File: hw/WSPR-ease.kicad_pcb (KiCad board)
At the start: 4 copper layers, 99 x 64 mm, 140 parts, among them J101 pwr+data, J102 SMA, J103 SMA, K201 G6K-2, K202 G6K-2, K203 G6K-2, Q101 MMBF170, Q201 MMBF170, Q202 MMBF170, Q203 MMBF170, Q401 MMBF170, Q402 MMBF170, Q403 MMBF170, Q404 MMBF170, Q405 MMBF170, Q406 MMBF170, Q501 MMBF170, Q502 MMBF170, Q503 MMBF170, Q504 MMBF170, Q505 MMBF170, Q506 MMBF170, T301 BN-43-202_DualPri_CTSec, U101 SRV05-4, U102 ESP32-S3-WROOM-1-N8R8, U103 LMR51430YDDCR, U104 GNSS module, U105 TPS74612PQWDRBRQ1, U106 TPS22918DBVR, U301 ICE40UP5K-SG48ITR, U401 UCC27524DGN, U501 UCC27524DGN, Y301 40MHz

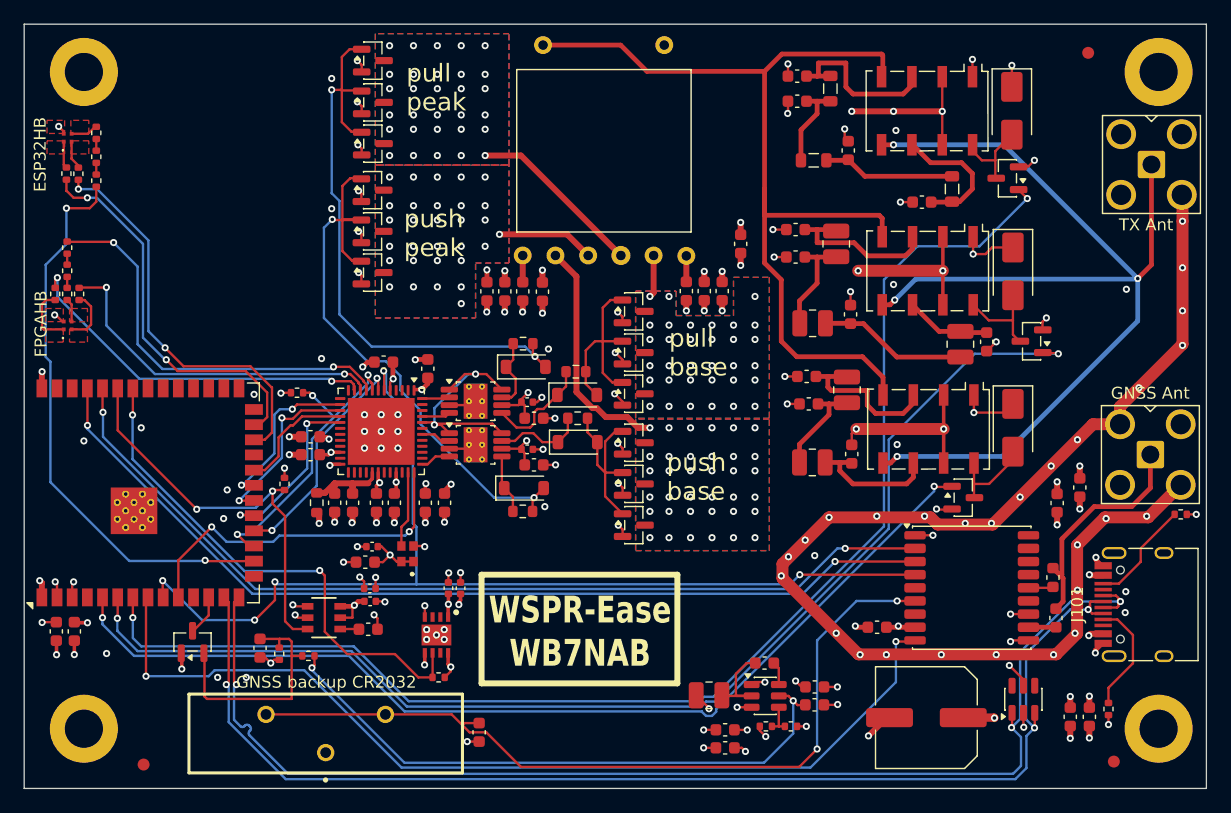
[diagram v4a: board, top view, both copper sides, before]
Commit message: Add symbols for new components, switch to SI5351 in place of FPGA. Simplify!
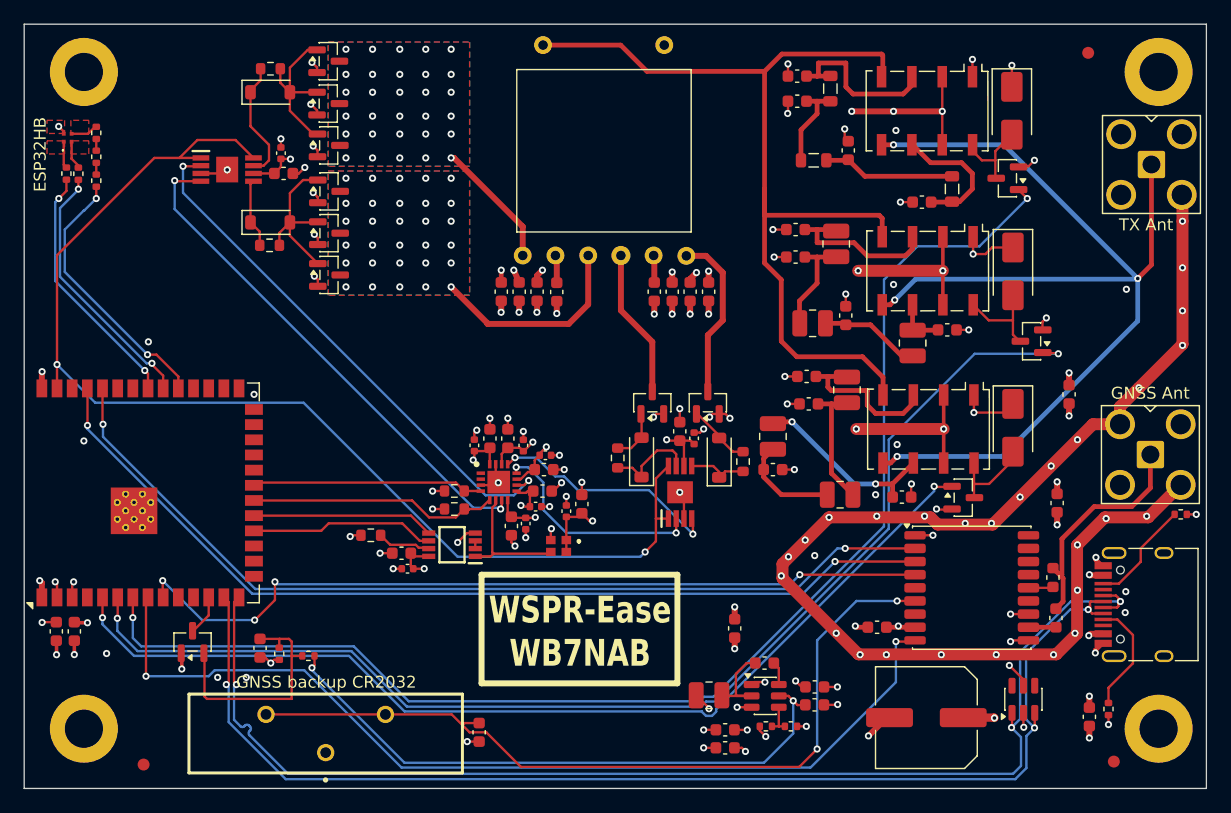
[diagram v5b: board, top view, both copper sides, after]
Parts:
- removed C115, C116, C401, C501: 1uF, Capacitor_SMD:C_0402_1005Metric
- removed C117: 1nF NP0 100V, Capacitor_SMD:C_0603_1608Metric
- removed the C206 at (118.8, 93.7)
- removed the C313 at (78.5, 116.7)
- removed the C314 at (86.1, 116.6)
- removed the C317 at (79.1, 109.5)
- removed the C318 at (84.8, 109.5)
- removed C402, C502: 100nF X7R 50V, Capacitor_SMD:C_0603_1608Metric
- removed D401, D402, D501, D502: 1N4148W, Diode_SMD:D_SOD-123
- removed the L205 at (128.0, 96.2)
- removed Q401, Q402, Q403, Q404, Q405, Q406, Q501, Q502, Q503, Q504, Q505, Q506: MMBF170, Package_TO_SOT_SMD:SOT-23
- removed the R110 at (84.3, 124.1)
- removed R113: 10k, Resistor_SMD:R_0402_1005Metric
- removed R401, R402, R501, R502: 10, Resistor_SMD:R_0603_1608Metric
- removed U105: TPS74612PQWDRBRQ1, Library:SON65P300X300X100-9N-D
- removed U106: TPS22918DBVR, Library:DBV6_TEX
- removed U401, U501: UCC27524DGN, Package_SO:Texas_DGN0008G_VSSOP-8-1EP_3x3mm_P0.65mm_EP2x2.94mm_Mask1.846x2.15mm_ThermalVias
- added C204: 910pF NP0 100V, Capacitor_SMD:C_0603_1608Metric, F.Cu at (123.1, 109.0)
- added C208: 330pF NP0 50V, Capacitor_SMD:C_0603_1608Metric, F.Cu at (126.9, 95.0)
- added C304: 1uF, Capacitor_SMD:C_0402_1005Metric, F.Cu at (81.7, 115.0)
- added C305: 100nF X7R 50V, Capacitor_SMD:C_0603_1608Metric, F.Cu at (81.2, 113.7)
- added C306: 1uF, Capacitor_SMD:C_0402_1005Metric, F.Cu at (71.1, 80.2)
- added C307: 100nF X7R 50V, Capacitor_SMD:C_0603_1608Metric, F.Cu at (71.3, 81.9)
- added C325: 100nF X7R 50V, Capacitor_SMD:C_0603_1608Metric, F.Cu at (90.1, 104.1)
- added C326: 1uF, Capacitor_SMD:C_0402_1005Metric, F.Cu at (91.4, 104.7)
- added C327: 100nF X7R 50V, Capacitor_SMD:C_0603_1608Metric, F.Cu at (93.1, 106.7)
- added C328: 1uF, Capacitor_SMD:C_0402_1005Metric, F.Cu at (93.2, 105.5)
- added D302: 1N4148W, Diode_SMD:D_SOD-123, F.Cu at (70.2, 75.1)
- added D303: 1N4148W, Diode_SMD:D_SOD-123, F.Cu at (107.8, 105.7)
- added D304: 1N4148W, Diode_SMD:D_SOD-123, F.Cu at (101.3, 105.7)
- added L203: 2.7uH, Inductor_SMD:L_1008_2520Metric, F.Cu at (112.3, 103.9)
- added L206: 1uH, Inductor_SMD:L_1008_2520Metric, F.Cu at (124.0, 96.1)
- added Q301: MMBF170, Package_TO_SOT_SMD:SOT-23, F.Cu at (75.1, 83.4)
- added Q302: MMBF170, Package_TO_SOT_SMD:SOT-23, F.Cu at (75.1, 86.9)
- added Q303: MMBF170, Package_TO_SOT_SMD:SOT-23, F.Cu at (75.1, 90.4)
- added Q304: MMBF170, Package_TO_SOT_SMD:SOT-23, F.Cu at (75.1, 72.5)
- added Q305: MMBF170, Package_TO_SOT_SMD:SOT-23, F.Cu at (75.1, 76.0)
- added Q306: MMBF170, Package_TO_SOT_SMD:SOT-23, F.Cu at (75.1, 79.5)
- added Q307: MMBF170, Package_TO_SOT_SMD:SOT-23, F.Cu at (106.8, 101.1)
- added Q308: MMBF170, Package_TO_SOT_SMD:SOT-23, F.Cu at (102.2, 101.1)
- added U302: UCC27525DGN, Library:SOP65P490X110-9N, F.Cu at (66.6, 81.6)
- added U303: UCC27525DGN, Library:SOP65P490X110-9N, F.Cu at (104.5, 108.6)
- added Y302: Si5351C-B-GM, Library:QFN50P300X300X90-17N-D, F.Cu at (89.3, 107.8)
- C201: value 470pF NP0 100V -> 910pF NP0 100V
- C202: value 1nF NP0 100V -> 1.6nF NP0 100V
- C203: value 470pF NP0 100V -> 1.6nF NP0 100V
- C205: renamed from C204; value 150pF NP0 100V -> 330pF NP0 50V
- C206: renamed from C205; value 330pF NP0 100V -> 560pF NP0 50V
- C207: value 150pF NP0 100V -> 560pF NP0 50V
- C315, C320: value 100nF X7R 50V -> 1uF; footprint Capacitor_SMD:C_0603_1608Metric -> Capacitor_SMD:C_0402_1005Metric
- C322, C324: value 10uF X5R 25V -> 1uF; footprint Capacitor_SMD:C_0603_1608Metric -> Capacitor_SMD:C_0402_1005Metric
- C323: value 10uF X5R 25V -> 100nF X7R 50V
- D301: value LED_BGRA -> 1N4148W; footprint Library:UHD111AFKAC3K23E1L3VG5ZB3Z3 -> Diode_SMD:D_SOD-123
- L201, L202: value 1.2uH -> 2.7uH
- L204: renamed from L203; value 560nH -> 1uH
- L205: renamed from L204; value 680nH -> 1.2uH
- R301, R303: value 100 -> 10; footprint Resistor_SMD:R_0402_1005Metric -> Resistor_SMD:R_0603_1608Metric
- R302: value 100 -> 10k; footprint Resistor_SMD:R_0402_1005Metric -> Resistor_SMD:R_0603_1608Metric
- R304, R305: value 100 -> 47; footprint Resistor_SMD:R_0402_1005Metric -> Resistor_SMD:R_0603_1608Metric
- R306: value 10k -> 5.1k; footprint Resistor_SMD:R_0402_1005Metric -> Resistor_SMD:R_0603_1608Metric
- R307: value 10 -> 5.1k
- U301: value ICE40UP5K-SG48ITR -> SN74LVC1G74DCTR; footprint Package_DFN_QFN:QFN-48-1EP_7x7mm_P0.5mm_EP5.6x5.6mm -> Library:SOP65P400X130-8N
- moved R304 57.3 mm to (109.8, 106.0), turned to 90 degrees
- moved R305 49.1 mm to (99.3, 105.7), turned to 90 degrees
- moved R302 33.7 mm to (78.6, 112.2), turned to 180 degrees
- moved C317 29.1 mm to (109.1, 120.0), turned to -90 degrees
- moved C315 26.8 mm to (105.7, 104.1), turned to -90 degrees
- moved R303 25.4 mm to (70.2, 73.1), turned to 0 degrees
- moved C316 21.7 mm to (104.5, 103.5)
- moved C324 19.7 mm to (92.4, 109.8)
- moved D301 19.0 mm to (70.2, 86.0), turned to 0 degrees
- moved C312 18.8 mm to (96.3, 109.6), turned to 90 degrees
- moved C321 17.9 mm to (90.4, 111.4), turned to -90 degrees
- moved R301 17.0 mm to (70.2, 87.9), turned to 0 degrees
- moved C311 16.5 mm to (95.0, 110.2), turned to 90 degrees
- moved R306 16.4 mm to (85.6, 110.0)
- moved C322 14.6 mm to (91.6, 111.2), turned to -90 degrees
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- renumbered C208 to C209, C209 to C210, C210 to C211, C211 to C212, C302 to C301, C303 to C302, C304 to C303, C310 to C308, C311 to C309, C312 to C310, C308 to C311, C309 to C312, C305 to C313, C301 to C314, C307 to C317, C306 to C318, L206 to L207, L207 to L208, L208 to L209, R111 to R110, R112 to R111
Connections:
- C311 pad 1: +VFPGAIO -> +3.3V
- C312 pad 1: +VFPGAIO -> +3.3V
- C315 pad 2: +VFPGACORE -> VBUS
- C316 pad 2: +VFPGAIO -> VBUS
- C319 pad 1: GND -> +3.3V
- C319 pad 2: Net-(U301D-VCCPLL) -> GND
- C320 pad 1: GND -> +3.3V
- C320 pad 2: +VFPGAIO -> GND
- C321 pad 1: GND -> +3.3V
- C321 pad 2: +VFPGAIO -> GND
- C322 pad 1: GND -> +3.3V
- C322 pad 2: Net-(U301D-VCCPLL) -> GND
- C323 pad 1: GND -> +3.3V
- C323 pad 2: +VFPGAIO -> GND
- C324 pad 1: GND -> +3.3V
- C324 pad 2: +VFPGAIO -> GND
- D301 pad 1: /Transmitter/blu -> Net-(D301-K)
- D301 pad 2: /Transmitter/grn -> Net-(D301-A)
- K201 pad 6: Net-(C203-Pad1) -> Net-(C204-Pad1)
- K202 pad 6: Net-(C207-Pad1) -> Net-(C208-Pad1)
- L205 pad 2: Net-(C206-Pad1) (its old number) -> Net-(C207-Pad1)
- R105 pad 1: Net-(U102-IO46) -> /hbRed
- R108 pad 1: Net-(U102-IO47) -> /hbGrn
- R109 pad 1: Net-(U102-IO48) -> /hbBlu
- R301 pad 1: /Transmitter/hbR -> Net-(D301-K)
- R301 pad 2: Net-(R301-Pad2) -> Net-(D301-A)
- R302 pad 1: Net-(R301-Pad2) -> Net-(U301-~{PRE})
- R302 pad 2: Net-(R302-Pad2) -> +3.3V
- R303 pad 1: Net-(R302-Pad2) -> Net-(D302-K)
- R303 pad 2: /Transmitter/red -> Net-(D302-A)
- R304 pad 1: /Transmitter/hbG -> Net-(D303-K)
- R304 pad 2: /Transmitter/grn -> Net-(D303-A)
- R305 pad 1: /Transmitter/hbB -> Net-(D304-K)
- R305 pad 2: /Transmitter/blu -> Net-(D304-A)
- R306 pad 1: /fpgaCRESET -> /txSDA
- R306 pad 2: GND -> +3.3V
- R307 pad 1: Net-(U301D-VCCPLL) -> /txSCL
- R307 pad 2: +VFPGACORE -> +3.3V
- T301 pad 1: VBUS -> /Transmitter/ahcPushT
- T301 pad 2: /Transmitter/pullBaseT -> VBUS
- T301 pad 3: /Transmitter/pullPeakT -> /Transmitter/ahcPullT
- T301 pad 4: /Transmitter/pushPeakT -> /Transmitter/txPullT
- T301 pad 5: /Transmitter/pushBaseT -> VBUS
- T301 pad 6: VBUS -> /Transmitter/txPushT
- U102 pad 10: /fpgaNRESET -> unconnected-(U102-IO17-Pad10)
- U102 pad 16: Net-(U102-IO46) -> unconnected-(U102-IO46-Pad16)
- U102 pad 17: /fpgaCRESET -> unconnected-(U102-IO9-Pad17)
- U102 pad 18: /fpgaDONE -> /txCLKen
- U102 pad 19: /fpgaMOSI -> /tcxoDiv2
- U102 pad 20: /fpgaSCLK -> /txSDA
- U102 pad 21: /fpgaMISO -> /txSCL
- U102 pad 22: /fpgaNCS -> unconnected-(U102-IO14-Pad22)
- U102 pad 24: Net-(U102-IO47) -> unconnected-(U102-IO47-Pad24)
- U102 pad 25: Net-(U102-IO48) -> unconnected-(U102-IO48-Pad25)
- U102 pad 31: unconnected-(U102-IO38-Pad31) -> /hbRed
- U102 pad 32: unconnected-(U102-IO39-Pad32) -> /hbGrn
- U102 pad 33: unconnected-(U102-IO40-Pad33) -> /hbBlu
- U102 pad 34: /pgFPGACORE -> unconnected-(U102-IO41-Pad34)
- U102 pad 35: /enFPGAIO -> unconnected-(U102-IO42-Pad35)
- U102 pad 39: unconnected-(U102-IO1-Pad39) -> /txPAen
- U301 pad 1: +VFPGAIO -> /Transmitter/tcxo
- U301 pad 2: unconnected-(U301C-IOB_6a-Pad2) -> Net-(U301-D)
- U301 pad 3: unconnected-(U301C-IOB_9b-Pad3) -> Net-(U301-D)
- U301 pad 4: unconnected-(U301C-IOB_8a-Pad4) -> GND
- U301 pad 5: +VFPGACORE -> /tcxoDiv2
- U301 pad 6: /gnssPPS -> /txCLKen
- U301 pad 7: /fpgaDONE -> Net-(U301-~{PRE})
- U301 pad 8: /fpgaCRESET -> +3.3V
- Y301 pad 1: +VFPGAIO -> +3.3V
- Y301 pad 3: /Transmitter/FPGACLK -> /Transmitter/tcxo
- Y301 pad 4: +VFPGAIO -> +3.3V
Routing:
- net /txPAen: track 0.00 -> 99.2 mm, vias 0 -> 2
- net Net-(D501-A): track 51.2 -> 0.00 mm, vias 2 -> 0
- net Net-(D402-A): track 49.5 -> 0.00 mm, vias 2 -> 0
- net Net-(U102-IO46): track 47.6 -> 0.00 mm, vias 2 -> 0
- net /Transmitter/txCLK1: track 0.00 -> 44.9 mm, vias 0 -> 2
- net /pgFPGACORE: track 43.5 -> 0.00 mm, vias 2 -> 0
- net /Transmitter/txCLK2: track 0.00 -> 43.1 mm, vias 0 -> 2
- net /Transmitter/hbR: track 34.5 -> 0.00 mm, vias 2 -> 0
- net /enFPGAIO: track 34.4 -> 0.00 mm, vias 2 -> 0
- net Net-(U102-IO47): track 33.9 -> 0.00 mm, vias 2 -> 0
- net Net-(U102-IO48): track 32.3 -> 0.00 mm, vias 2 -> 0
- net /Transmitter/hbB: track 30.9 -> 0.00 mm, vias 2 -> 0
- net /fpgaNRESET: track 29.6 -> 0.00 mm, vias 2 -> 0
- net /Transmitter/hbG: track 29.3 -> 0.00 mm, vias 2 -> 0
- net /fpgaCRESET: track 24.8 -> 0.00 mm, vias 3 -> 0
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- added copper zone on B.Cu, net /Transmitter/txPullT
- added copper zone on F.Cu, net /Transmitter/txPullT
- added copper zone on B.Cu, net /Transmitter/txPushT
- added copper zone on F.Cu, net /Transmitter/txPushT
- removed copper zone on In2.Cu, net +VFPGACORE
- removed copper zone on In2.Cu, net +VFPGAIO
- removed copper zone on F.Cu, net /Transmitter/blu
- removed copper zone on F.Cu, net /Transmitter/grn
- removed copper zone on B.Cu, net /Transmitter/pullBaseT
- removed copper zone on F.Cu, net /Transmitter/pullBaseT
- removed copper zone on B.Cu, net /Transmitter/pullPeakT
- removed copper zone on F.Cu, net /Transmitter/pullPeakT
- removed copper zone on B.Cu, net /Transmitter/pushBaseT
- removed copper zone on F.Cu, net /Transmitter/pushBaseT
- removed copper zone on B.Cu, net /Transmitter/pushPeakT
- removed copper zone on F.Cu, net /Transmitter/pushPeakT
- removed copper zone on F.Cu, net /Transmitter/red
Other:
- board text removed: "pull base"
- board text removed: "pull peak"
- board text removed: "push base"
- board text removed: "push peak"

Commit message: Switch to SI5351C-B-GM for exciter + AHC to attenuate 3rd harmonic on a separate winding on the binocular transformer. Do so layout tweaks. This is much simpler than the FPGA version.
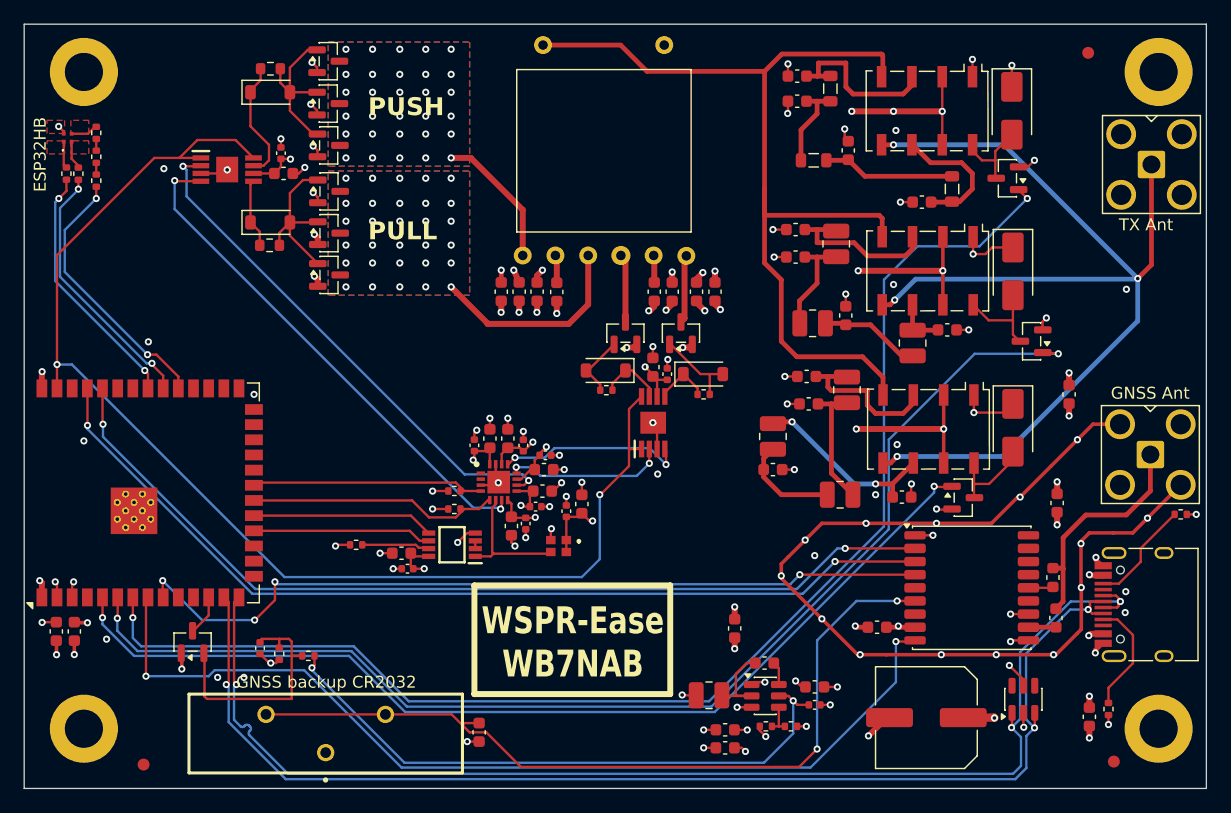
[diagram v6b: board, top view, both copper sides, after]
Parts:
- C106: value 1nF NP0 100V -> 1uF X7R 25V; footprint Capacitor_SMD:C_0603_1608Metric -> Capacitor_SMD:C_0402_1005Metric
- C112: footprint Capacitor_SMD:C_0603_1608Metric -> Capacitor_SMD:C_0402_1005Metric
- C304, C311, C320, C322, C324, C326, C328: value 1uF -> 1uF X7R 25V
- C305: renamed from C306; value 1uF -> 1uF X7R 25V
- C313: renamed from C315; value 1uF -> 1uF X7R 25V
- R302: value 10k -> 22.1k; footprint Resistor_SMD:R_0603_1608Metric -> Resistor_SMD:R_0402_1005Metric
- R304, R305, R306, R307: footprint Resistor_SMD:R_0603_1608Metric -> Resistor_SMD:R_0402_1005Metric
- moved D304 7.87 mm to (98.3, 98.4), turned to 180 degrees
- moved D303 7.13 mm to (106.5, 98.7), turned to 0 degrees
- moved R304 6.52 mm to (106.5, 100.4), turned to 0 degrees
- moved Q307 6.24 mm to (104.6, 95.3)
- moved Q308 6.24 mm to (100.0, 95.3)
- moved U303 6.24 mm to (102.3, 102.8)
- moved C313 5.83 mm to (103.5, 98.7)
- moved C316 5.83 mm to (102.2, 98.1)
- moved R305 5.75 mm to (98.3, 100.0), turned to 180 degrees
- moved R302 1.46 mm to (77.4, 113.0)
- moved C308 0.54 mm to (105.9, 91.8)
- moved C314 0.54 mm to (107.5, 91.8)
- renumbered C305 to C306, C313 to C314, C314 to C315, Y302 to U304
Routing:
- net GND: track 230.7 -> 207.5 mm, vias 129 -> 117
- net /Transmitter/ahcPushT: track 14.1 -> 5.72 mm
- net /Transmitter/ahcPullT: track 12.5 -> 5.72 mm
- net /Transmitter/ahcCLK2: track 18.7 -> 13.6 mm
- net /txPAen: track 99.2 -> 103.6 mm
- net /Transmitter/ahcCLK1: track 19.6 -> 15.6 mm
- net Net-(D304-K): track 7.81 -> 5.43 mm
- net Net-(D303-A): track 5.05 -> 7.18 mm
- net /Transmitter/txCLK1: track 44.9 -> 43.8 mm
- net Net-(D304-A): track 4.30 -> 5.40 mm
- net Net-(U301-~{PRE}): track 4.71 -> 5.73 mm
- net /txCLKen: track 15.9 -> 15.0 mm
- net /Transmitter/txPushT: track 10.8 -> 11.6 mm
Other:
- board text added: "PULL"
- board text added: "PUSH"

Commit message: Horsing around with JLCPCB assembly and BOM. I think it is still too expensive to do it this way for p1 build
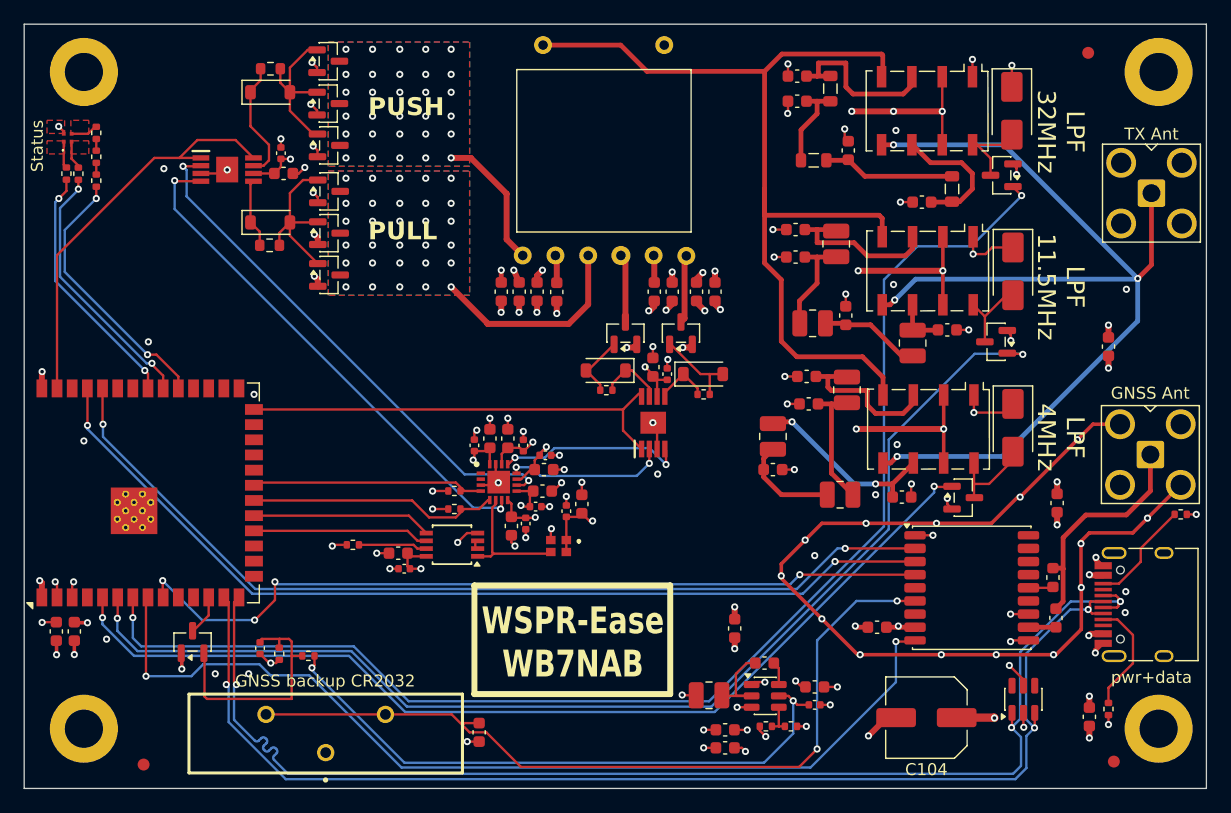
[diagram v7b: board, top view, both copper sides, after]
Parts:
- C104: footprint Capacitor_SMD:C_Elec_8x6.2 -> Capacitor_SMD:C_Elec_6.3x7.7
- C106, C112, C304, C305, C311, C313, C320: value 1uF X7R 25V -> 1uF X5R 25V
- C108, C303, C308: value 100pF NP0 100V -> 100pF NP0 50V
- C201, C204: value 910pF NP0 100V -> 910pF NP0 50V
- C202, C203: value 1.6nF NP0 100V -> 1.6nF NP0 50V
- C209, C212: value 82pF NP0 100V -> 82pF NP0 50V
- C210, C211: value 180pF NP0 100V -> 180pF NP0 50V
- C322: renamed from C324; value 1uF X7R 25V -> 1uF X5R 25V
- C324: renamed from C328; value 1uF X7R 25V -> 1uF X5R 25V
- C326: renamed from C322; value 1uF X7R 25V -> 1uF X5R 25V
- C328: renamed from C326; value 1uF X7R 25V -> 1uF X5R 25V
- U301: footprint Library:SOP65P400X130-8N -> Package_SO:TSSOP-8_3x3mm_P0.65mm
- U304: value Si5351C-B-GM -> Si5351C-B-GM1
- moved C318 5.19 mm to (140.4, 96.4)
- moved Q202 2.98 mm to (131.0, 96.0)
- moved J102 2.40 mm to (144.0, 83.5)
- moved Q203 0.54 mm to (131.5, 82.0)
- moved C304 0.28 mm to (81.4, 115.0)
- moved C306 0.28 mm to (80.9, 113.7)
- moved R302 0.28 mm to (77.1, 113.0)
- renumbered C323 to C321, C327 to C323, C321 to C325, C325 to C327
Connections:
- U102 pad 26: unconnected-(U102-IO45-Pad26) -> /ahcEn
- U303 pad 1: /txPAen -> /ahcEn
- U303 pad 8: /txPAen -> /ahcEn
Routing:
- net /txPAen: track 103.6 -> 34.0 mm, vias 2 -> 0
- net /ahcEn: track 0.00 -> 36.7 mm
- net /midON: track 102.2 -> 99.3 mm
- net /Low Pass Filters/RFout: track 88.2 -> 85.8 mm
- net /D+: track 104.3 -> 105.8 mm
- net Net-(D202-A): track 8.01 -> 6.59 mm
- net GND: track 207.5 -> 206.4 mm
- net +3.3V: track 46.6 -> 46.0 mm
- net VBUS: track 93.6 -> 93.0 mm
- net Net-(D203-A): track 6.40 -> 7.04 mm
- net /Transmitter/ahcPullT: track 5.72 -> 5.19 mm
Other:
- board text added: "LPF 11.5MHz"
- board text added: "LPF 32MHz"
- board text added: "LPF 4MHz"

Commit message: OCD fixes. Fix USB2 connector footprint AGAIN (these things are not standardized!).
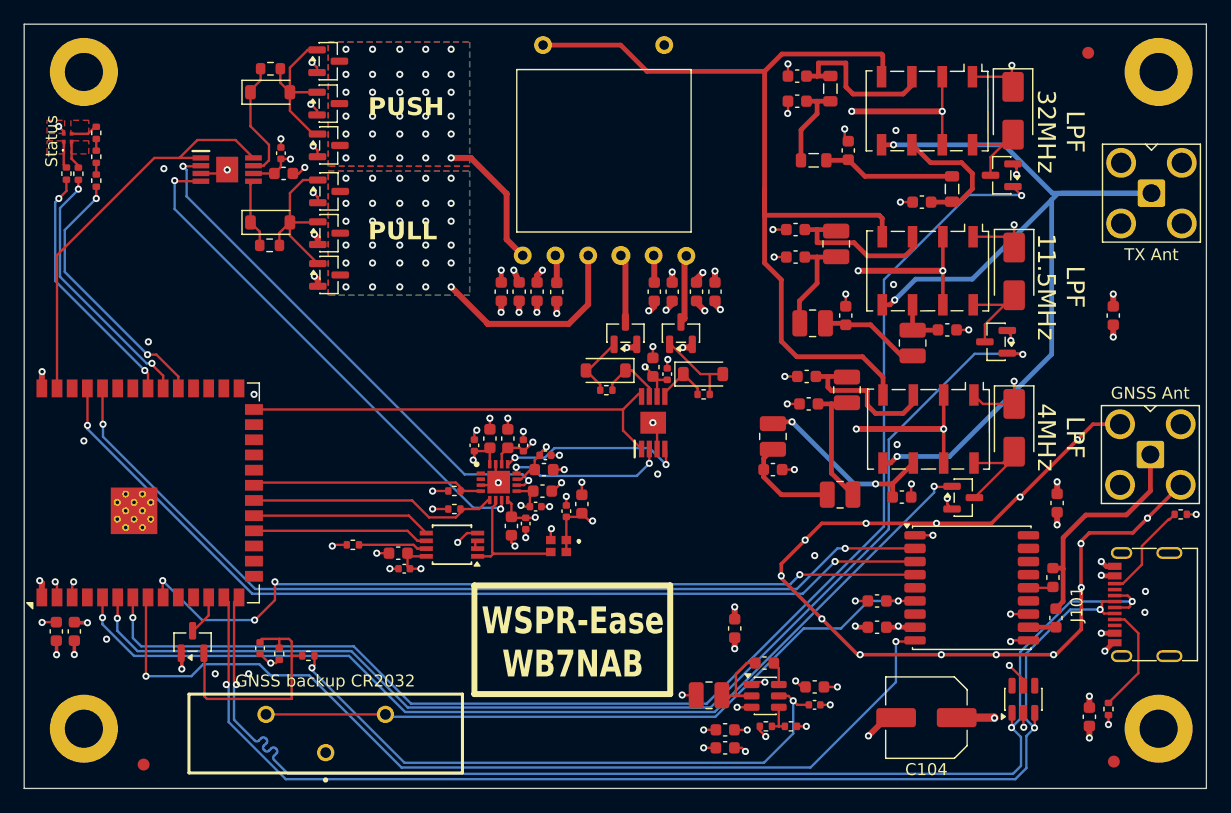
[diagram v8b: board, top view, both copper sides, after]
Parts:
- C108, C303, C308: value 100pF NP0 50V -> 100pF NP0 100V
- C201, C204: value 910pF NP0 50V -> 910pF NP0 100V
- C202, C203: value 1.6nF NP0 50V -> 1.6nF NP0 63V
- J101: footprint Library:USB_C_Receptacle_HRO_TYPE-C-31-M-12-bursted -> Library:UJ20-C-H-G-SMT-P16-TR
- moved C107 35.1 mm to (121.0, 117.7), turned to 0 degrees
- moved J101 3.60 mm to (147.6, 118.0)
- moved C318 2.63 mm to (140.8, 93.8)
- moved D201 0.10 mm to (132.5, 103.2)
- moved D202 0.10 mm to (132.5, 90.1)
- moved D203 0.10 mm to (132.4, 76.7)
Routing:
- net Net-(U104-V_BCKP): track 68.7 -> 59.4 mm, vias 2 -> 1
- net /Low Pass Filters/RFout: track 85.8 -> 81.3 mm, vias 4 -> 3
- net VBUS: track 93.0 -> 97.4 mm, vias 23 -> 22
- net Net-(D203-A): track 7.04 -> 9.12 mm
- net Net-(D201-A): track 6.94 -> 8.46 mm
- net /D-: track 101.6 -> 102.6 mm
- net /D+: track 105.8 -> 106.8 mm
- net Net-(D202-A): track 6.59 -> 7.54 mm
- net GND: vias 117 -> 114
